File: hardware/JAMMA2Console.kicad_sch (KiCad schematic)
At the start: 37 parts, among them J1 Conn_02x28_JAMMA, J13 Conn_01x03, J2 DS1038-15FBNSiA74-0CC, J3 SCART-F, J4 DF1BZ-34DP-2.5DSA, J5 PJ-320D, J6 DS1037-15FNAKT74-0CC, J7 DS1037-15FNAKT74-0CC, J8 Phoenix PTS 1,5/4-5.0, J9 Molex 67503-1020, U1 USBLC6-2P6, U2 LD1117-3.3

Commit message: Pushing work I did a few months ago and I forgot to push. Identified some mistakes which I'll fix in a future commit.
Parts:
- removed J13: Conn_01x03, Connector_PinHeader_2.54mm:PinHeader_1x03_P2.54mm_Vertical, symbol Connector_Generic:Conn_01x03
- JP3: footprint Jumper:SolderJumper-2_P1.3mm_Bridged2Bar_Pad1.0x1.5mm -> Jumper:SolderJumper-2_P1.3mm_Open_TrianglePad1.0x1.5mm
- R30: footprint Resistor_SMD:R_0402_1005Metric -> Resistor_SMD:R_0603_1608Metric
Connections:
- net Digital I/O/VCC: now also JP3.2; no longer JP3.1
- net at J6.1, J7.1: now also JP3.1; no longer JP3.2
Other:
- sheet Audio ports: added none; removed Audio_Select_~Mono~_Stereo
- sheet Digital I/O ports: added ~Mono_Shutdown~, ~Stereo_Shutdown~; removed Audio_Select_~Mono~_Stereo, UART_RX, UART_TX
- note added: "3V3 Regulator & Heatsink"
- note added: "Audio Amplifier Controls"
- note added: "Circuit Board Extras"
- note added: "JAMMA & External Controller Inputs"
- note added: "MISTAKE!!! UPDATE THE LAYOUT TO REFLECT THAT THIS IS A MALE CONNECTOR, AND CHECK THE NEO GEO PINOUT AGAIN, I HAVE EITHER PIN 9 MIRRORED, OR VCC & GND MIRRORED!!!"
- note added: "SCART Video & Audio Input"
- note added: "TO DO LIST: - Potentiometers for video signal? Might just rely on ones integrated on the monitor?"
- note added: "VGA Video Input"
- note added: "Video Input"
- note added: "Video Input Selection"
- note added: "Video Selection Controls"
- note removed: "TO DO LIST: - Potentiometers for video signal? Might just rely on ones integrated on the monitor? - Eventually swap audio control IC to M62429 (In Revision 2)"
- moved on the sheet: C1, C2, D1, D10, D12, D13, D2, D3, D4, D5, D6, D7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

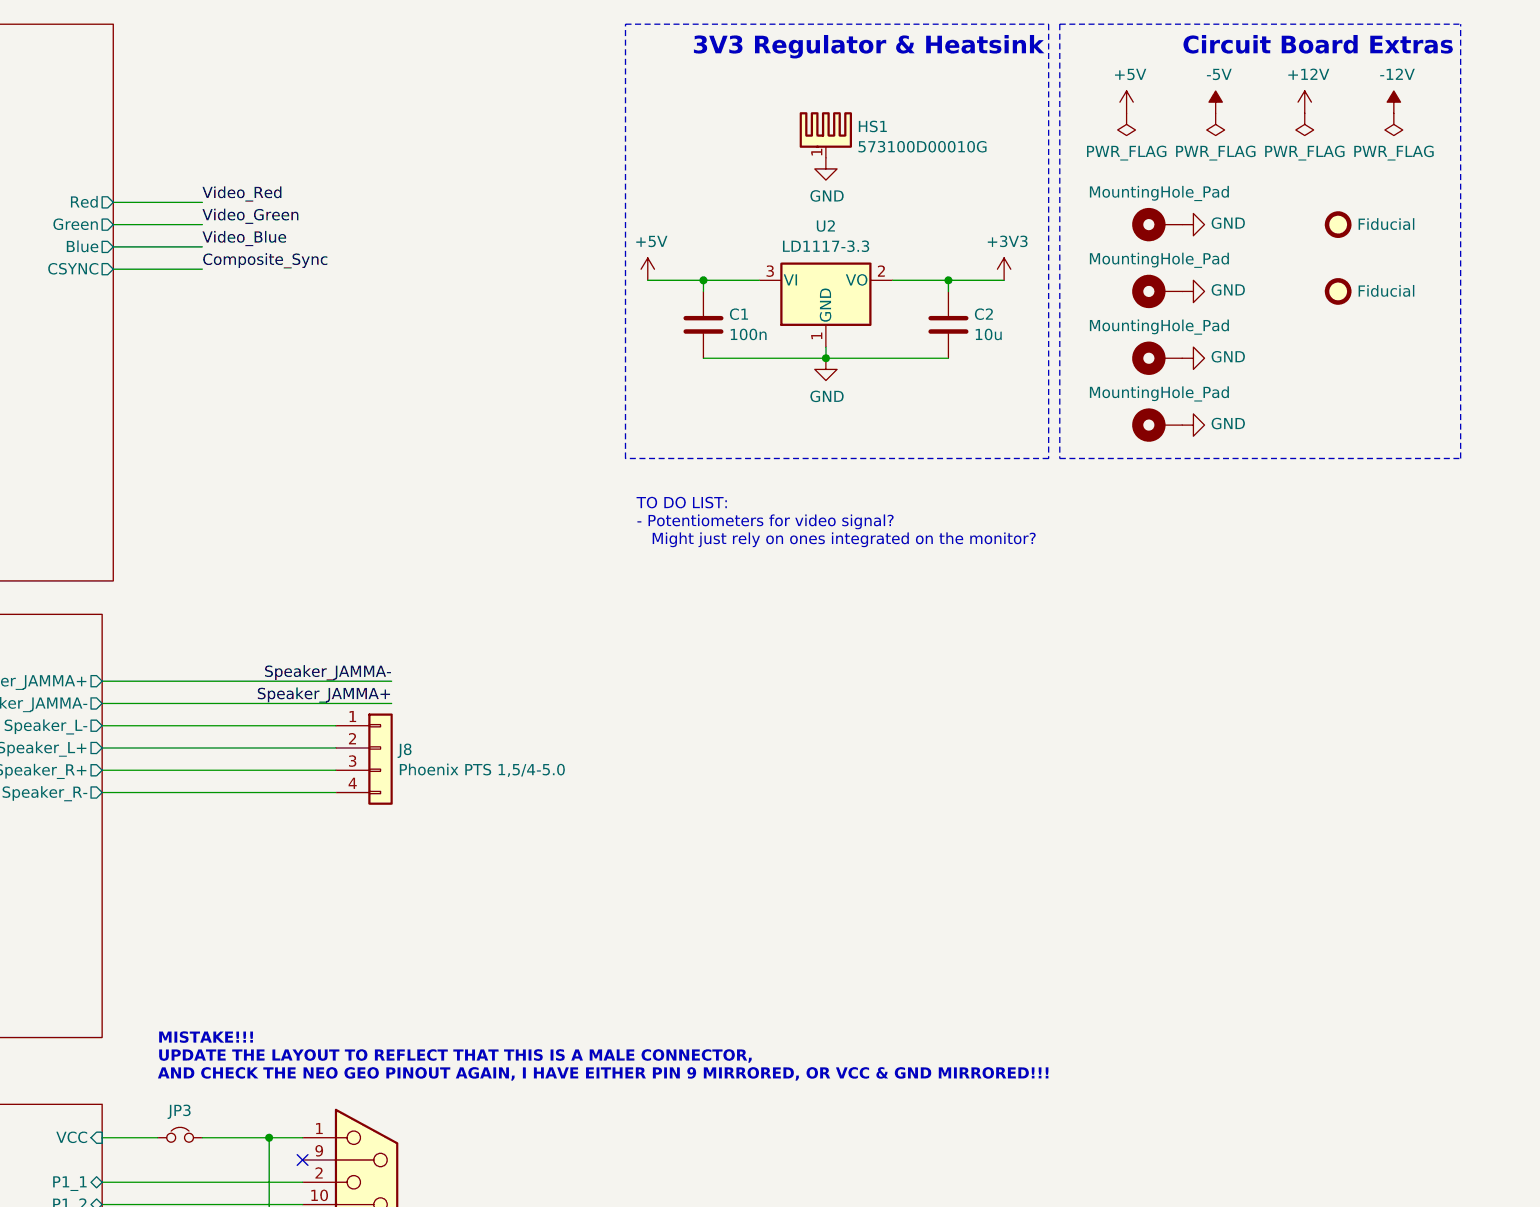
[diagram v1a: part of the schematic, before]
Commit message: Updated the schematic & layout to fix the heat sink net issues with the 3v3 regulator.
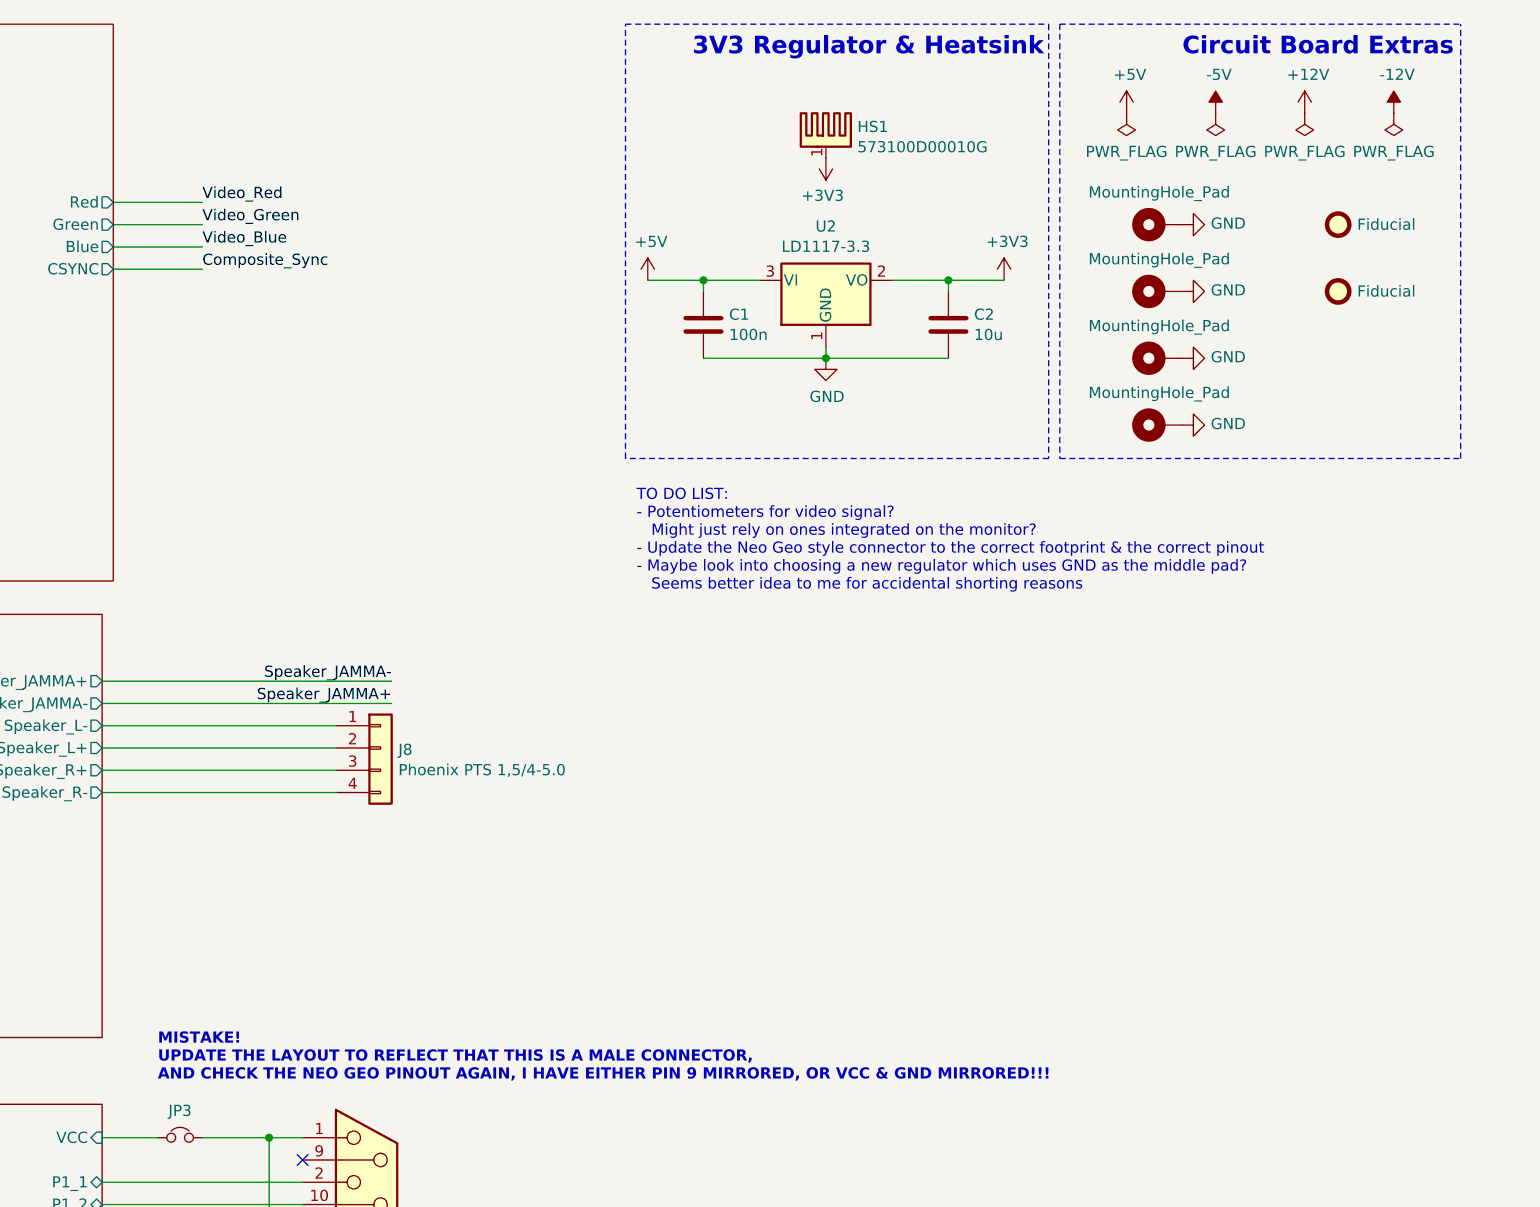
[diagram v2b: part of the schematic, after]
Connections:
- net +3V3: now also HS1.1
- net GND: no longer HS1.1
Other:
- note added: "MISTAKE! UPDATE THE LAYOUT TO REFLECT THAT THIS IS A MALE CONNECTOR, AND CHECK THE NEO GEO PINOUT AGAIN, I HAVE EITHER PIN 9 MIRRORED, OR VCC & GND MIRRORED!!!"
- note added: "TO DO LIST: - Potentiometers for video signal? Might just rely on ones integrated on the monitor? - Update the Neo Geo style connector to the correct footprint & the correct pinout - Maybe look into choosing a new regulator which uses GND as the middle pad? Seems better idea to me for accidental shorting reasons"
- note removed: "MISTAKE!!! UPDATE THE LAYOUT TO REFLECT THAT THIS IS A MALE CONNECTOR, AND CHECK THE NEO GEO PINOUT AGAIN, I HAVE EITHER PIN 9 MIRRORED, OR VCC & GND MIRRORED!!!"
- note removed: "TO DO LIST: - Potentiometers for video signal? Might just rely on ones integrated on the monitor?"
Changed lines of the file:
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@@
   (junction (at 289.56 53.34))
   (junction (at 303.53 44.45))
+  (no_connect (at 77.47 59.69))
+  (no_connect (at 69.85 121.92))
+  (no_connect (at 48.26 199.39))
+  (no_connect (at 82.55 181.61))
+  (no_connect (at 46.99 36.83))
+  (no_connect (at 82.55 201.93))
+  (no_connect (at 77.47 64.77))
+  (no_connect (at 77.47 54.61))
+  (no_connect (at 48.26 191.77))
+  (no_connect (at 82.55 196.85))
+  (no_connect (at 262.89 261.62))
+  (no_connect (at 95.25 201.93))
+  (no_connect (at 95.25 196.85))
+  (no_connect (at 95.25 171.45))
+  (no_connect (at 35.56 191.77))
+  (no_connect (at 82.55 168.91))
+  (no_connect (at 69.85 137.16))
+  (no_connect (at 95.25 176.53))
+  (no_connect (at 95.25 168.91))
+  (no_connect (at 95.25 173.99))
   (no_connect (at 48.26 201.93))
-  (no_connect (at 95.25 171.45))
+  (no_connect (at 95.25 184.15))
+  (no_connect (at 229.87 144.78))
+  (no_connect (at 46.99 82.55))
+  (no_connect (at 95.25 166.37))
+  (no_connect (at 95.25 194.31))
+  (no_connect (at 35.56 184.15))
+  (no_connect (at 35.56 186.69))
+  (no_connect (at 95.25 189.23))
+  (no_connect (at 82.55 166.37))
   (no_connect (at 95.25 191.77))
+  (no_connect (at 48.26 186.69))
+  (no_connect (at 95.25 179.07))
+  (no_connect (at 95.25 199.39))
+  (no_connect (at 82.55 199.39))
+  (no_connect (at 95.25 181.61))
+  (no_connect (at 35.56 201.93))
+  (no_connect (at 54.61 132.08))
+  (no_connect (at 95.25 186.69))
+  (no_connect (at 69.85 116.84))
+  (no_connect (at 82.55 179.07))
+  (no_connect (at 77.47 44.45))
+  (no_connect (at 46.99 77.47))
   (no_connect (at 82.55 173.99))
-  (no_connect (at 77.47 64.77))
-  (no_connect (at 82.55 166.37))
-  (no_connect (at 229.87 144.78))
-  (no_connect (at 48.26 186.69))
-  (no_connect (at 77.47 44.45))
-  (no_connect (at 54.61 132.08))
-  (no_connect (at 35.56 201.93))
-  (no_connect (at 262.89 261.62))
-  (no_connect (at 77.47 54.61))
-  (no_connect (at 82.55 168.91))
-  (no_connect (at 69.85 121.92))
+  (no_connect (at 48.26 184.15))
+  (no_connect (at 54.61 129.54))
+  (no_connect (at 95.25 204.47))
+  (no_connect (at 229.87 193.04))
   (no_connect (at 82.55 171.45))
-  (no_connect (at 35.56 191.77))
-  (no_connect (at 46.99 36.83))
-  (no_connect (at 95.25 179.07))
-  (no_connect (at 95.25 201.93))
-  (no_connect (at 95.25 181.61))
-  (no_connect (at 95.25 194.31))
-  (no_connect (at 95.25 204.47))
-  (no_connect (at 95.25 199.39))
-  (no_connect (at 82.55 181.61))
-  (no_connect (at 229.87 193.04))
-  (no_connect (at 95.25 196.85))
-  (no_connect (at 46.99 77.47))
-  (no_connect (at 82.55 201.93))
-  (no_connect (at 82.55 199.39))
-  (no_connect (at 48.26 191.77))
-  (no_connect (at 95.25 184.15))
-  (no_connect (at 82.55 196.85))
-  (no_connect (at 48.26 199.39))
-  (no_connect (at 95.25 189.23))
-  (no_connect (at 35.56 186.69))
-  (no_connect (at 82.55 179.07))
-  (no_connect (at 69.85 137.16))
-  (no_connect (at 95.25 173.99))
-  (no_connect (at 95.25 168.91))
-  (no_connect (at 54.61 129.54))
-  (no_connect (at 77.47 59.69))
-  (no_connect (at 95.25 186.69))
-  (no_connect (at 35.56 184.15))
-  (no_connect (at 46.99 82.55))
-  (no_connect (at 48.26 184.15))
-  (no_connect (at 95.25 176.53))
-  (no_connect (at 95.25 166.37))
-  (no_connect (at 69.85 116.84))
   (wire (pts (xy 19.05 179.07) (xy 19.05 166.37))
     (stroke (width 0) (type solid) (color 0 0 0 0))
@@
     (effects (font (size 1.27 1.27)) (justify right bottom))
   )
-  (text "MISTAKE!!!\nUPDATE THE LAYOUT TO REFLECT THAT THIS IS A MALE CONNECTOR,\nAND CHECK THE NEO GEO PINOUT AGAIN, I HAVE EITHER PIN 9 MIRRORED, OR VCC & GND MIRRORED!!!"
+  (text "MISTAKE!\nUPDATE THE LAYOUT TO REFLECT THAT THIS IS A MALE CONNECTOR,\nAND CHECK THE NEO GEO PINOUT AGAIN, I HAVE EITHER PIN 9 MIRRORED, OR VCC & GND MIRRORED!!!"
     (at 213.36 135.89 0)
     (effects (font (size 1.27 1.27) (thickness 0.254) bold) (justify left bottom))
   )
-  (text "TO DO LIST:\n- Potentiometers for video signal?\n   Might just rely on ones integrated on the monitor?"
-    (at 267.97 74.93 0)
+  (text "TO DO LIST:\n- Potentiometers for video signal?\n   Might just rely on ones integrated on the monitor?\n- Update the Neo Geo style connector to the correct footprint & the correct pinout\n- Maybe look into choosing a new regulator which uses GND as the middle pad?\n   Seems better idea to me for accidental shorting reasons"
+    (at 267.97 80.01 0)
     (effects (font (size 1.27 1.27)) (justify left bottom))
   )
@@
     )
   )
+  (symbol (lib_id "power:+3V3") (at 289.56 30.48 180) (unit 1)
+    (in_bom yes)
+    (property "Reference" "#PWR0160" (id 0) (at 289.56 26.67 0)
+      (effects (font (size 1.27 1.27)) hide)
+    )
+    (property "Value" "+3V3" (id 1) (at 289.1917 34.8044 0))
+    (property "Footprint" "" (id 2) (at 289.56 30.48 0)
+      (effects (font (size 1.27 1.27)) hide)
+    )
+    (property "Datasheet" "" (id 3) (at 289.56 30.48 0)
+      (effects (font (size 1.27 1.27)) hide)
+    )
+  )
   (symbol (lib_id "power:+3V3") (at 309.88 44.45 0) (unit 1)
     (in_bom yes)
@@
     )
     (property "Datasheet" "" (id 3) (at 270.51 278.13 0)
-      (effects (font (size 1.27 1.27)) hide)
-    )
-  )
-  (symbol (lib_id "power:GND") (at 289.56 30.48 0) (unit 1)
-    (in_bom yes)
-    (property "Reference" "#PWR0160" (id 0) (at 289.56 36.83 0)
-      (effects (font (size 1.27 1.27)) hide)
-    )
-    (property "Value" "GND" (id 1) (at 289.687 34.8742 0))
-    (property "Footprint" "" (id 2) (at 289.56 30.48 0)
-      (effects (font (size 1.27 1.27)) hide)
-    )
-    (property "Datasheet" "" (id 3) (at 289.56 30.48 0)
       (effects (font (size 1.27 1.27)) hide)
     )
@@
       (reference "#PWR0156") (unit 1)
     )
-    (path "/00000000-0000-0000-0000-00005eb366a6"
+    (path "/c24500b5-ee1a-4d61-8ef7-1562c5bcabdb"
       (reference "#PWR0160") (unit 1)
     )
